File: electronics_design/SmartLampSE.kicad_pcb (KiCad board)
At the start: 2 copper layers, 15 parts, among them J1 Screw_Terminal_01x02, M1 PIC16F886-IP, U1 L7805, Y1 Crystal

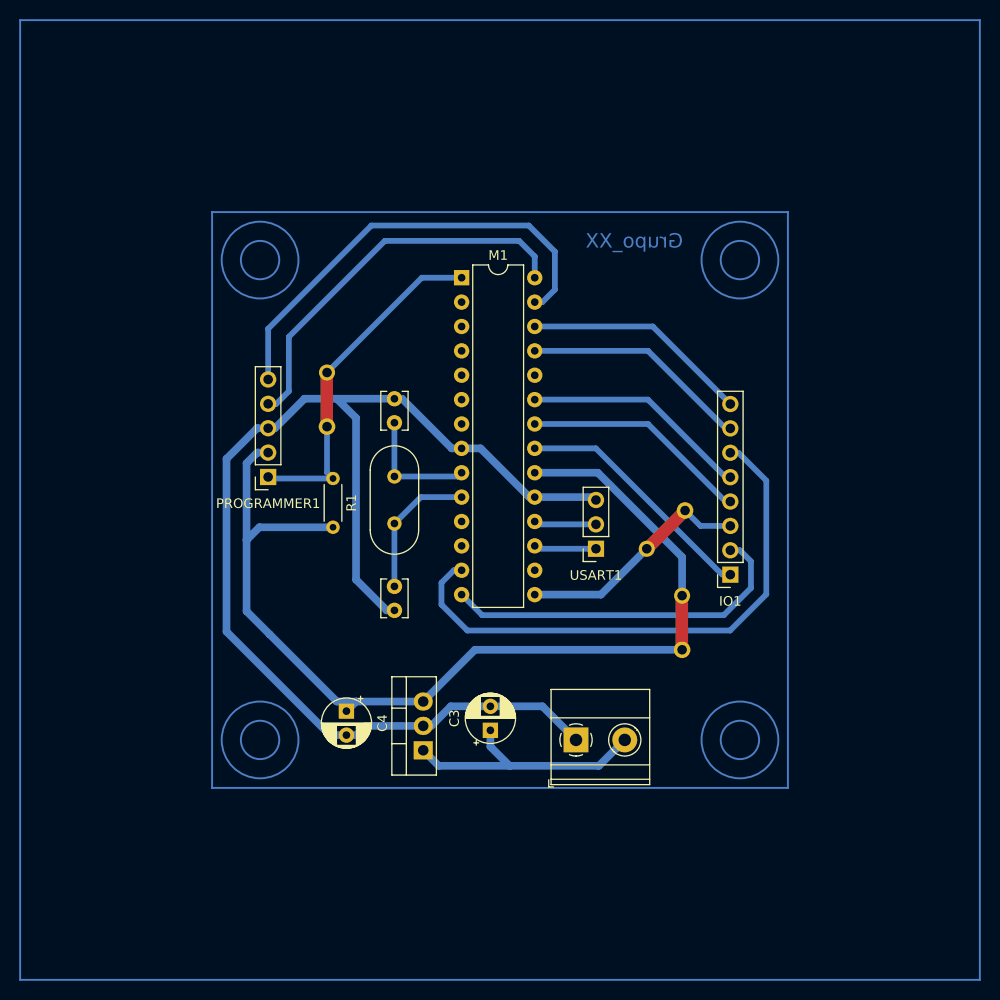
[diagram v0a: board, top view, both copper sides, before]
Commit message: Separate board IO interface
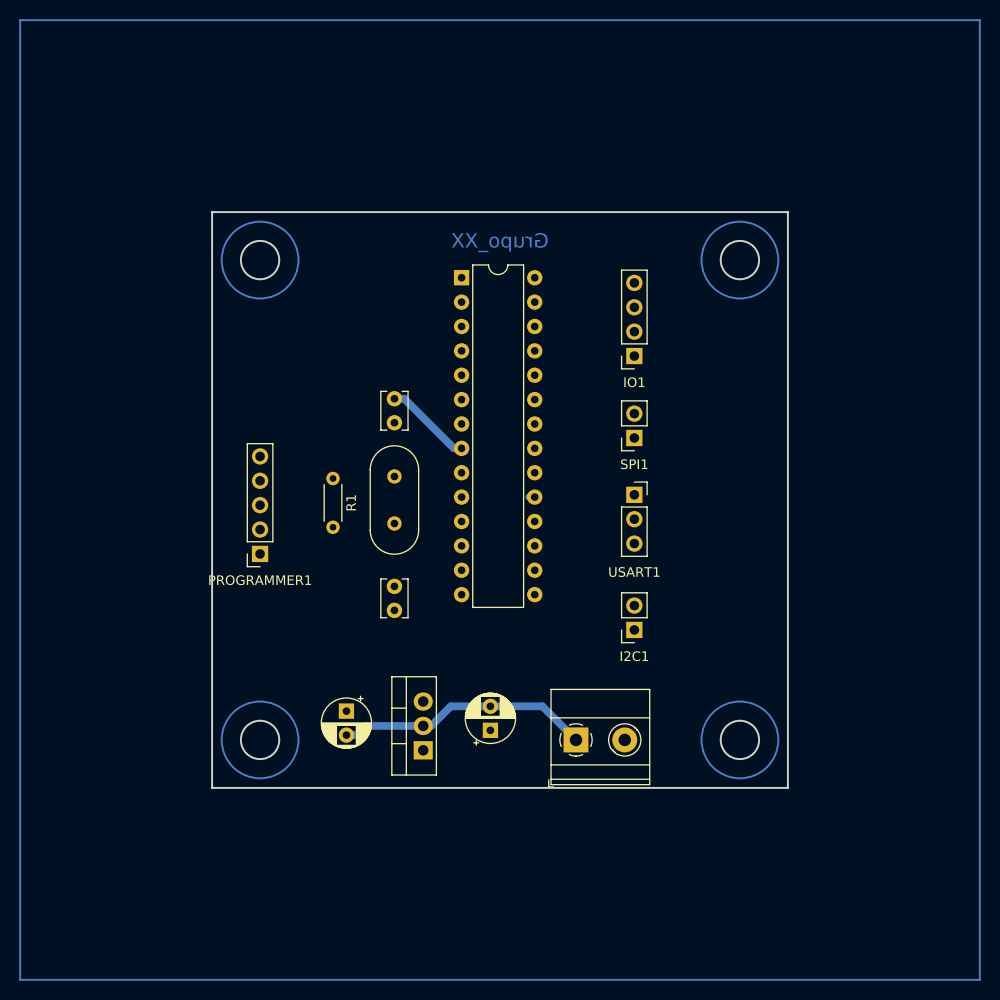
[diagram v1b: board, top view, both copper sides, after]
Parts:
- removed NT1, NT3: NetTie_2, Custom_Library:NetTie-2_THT_Custom_Pad1.0mm
- removed NT2: NetTie_2, NetTie:NetTie-2_THT_Pad1.0mm
- added I2C1: Conn_01x02, Connector_PinSocket_2.54mm:PinSocket_1x02_P2.54mm_Vertical, F.Cu at (155.0, 117.5)
- added SPI1: Conn_01x02, Connector_PinSocket_2.54mm:PinSocket_1x02_P2.54mm_Vertical, F.Cu at (155.0, 97.5)
- IO1: value Conn_01x08 -> Conn_01x04; footprint Connector_PinSocket_2.54mm:PinSocket_1x08_P2.54mm_Vertical -> Connector_PinSocket_2.54mm:PinSocket_1x04_P2.54mm_Vertical
- moved IO1 24.9 mm to (155.0, 89.0)
- moved PROGRAMMER1 8.06 mm to (116.0, 109.6)
- moved USART1 6.90 mm to (155.0, 103.5), turned to 0 degrees
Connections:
- M1 pad 1: Net-(M1-RE3/~{MCLR}/Vpp) -> mclr
- M1 pad 13: Net-(IO1-Pin_6) -> Net-(IO1-Pin_4)
- M1 pad 14: Net-(IO1-Pin_2) -> Net-(I2C1-Pin_1)
- M1 pad 20: Net-(M1-VDD) -> +5V
- M1 pad 22: Net-(IO1-Pin_4) -> Net-(IO1-Pin_2)
- M1 pad 23: Net-(IO1-Pin_5) -> Net-(IO1-Pin_3)
- M1 pad 25: Net-(IO1-Pin_7) -> Net-(M1-P1D/AN11/RB4)
- M1 pad 26: Net-(IO1-Pin_8) -> Net-(M1-~{T1G}/AN13/RB5)
- USART1 pad 1: Net-(M1-RC6/TX/CK) -> GND
- USART1 pad 3: GND -> Net-(M1-RC6/TX/CK)
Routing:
- net GND: track 132.1 -> 36.3 mm
- net +5V: track 80.6 -> 0.00 mm
- net Net-(IO1-Pin_6): track 58.3 -> 0.00 mm
- net icsp_clk: track 47.3 -> 0.00 mm
- net icsp_dat: track 41.0 -> 0.00 mm
- net Net-(IO1-Pin_2): track 37.6 -> 0.00 mm
- net +12V: track 27.3 -> 0.00 mm
- net Net-(IO1-Pin_1): track 25.8 -> 0.00 mm
- net Net-(IO1-Pin_7): track 23.7 -> 0.00 mm
- net Net-(IO1-Pin_8): track 23.7 -> 0.00 mm
- net Net-(IO1-Pin_5): track 23.7 -> 0.00 mm
- net Net-(IO1-Pin_4): track 23.7 -> 0.00 mm
- net Net-(M1-VDD): track 23.0 -> 0.00 mm
- net Net-(M1-RE3/~{MCLR}/Vpp): track 18.1 -> 0.00 mm
- net Net-(M1-CLKOUT/OSC2/RA6): track 14.7 -> 0.00 mm
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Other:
- board outline added: 60 x 60 mm

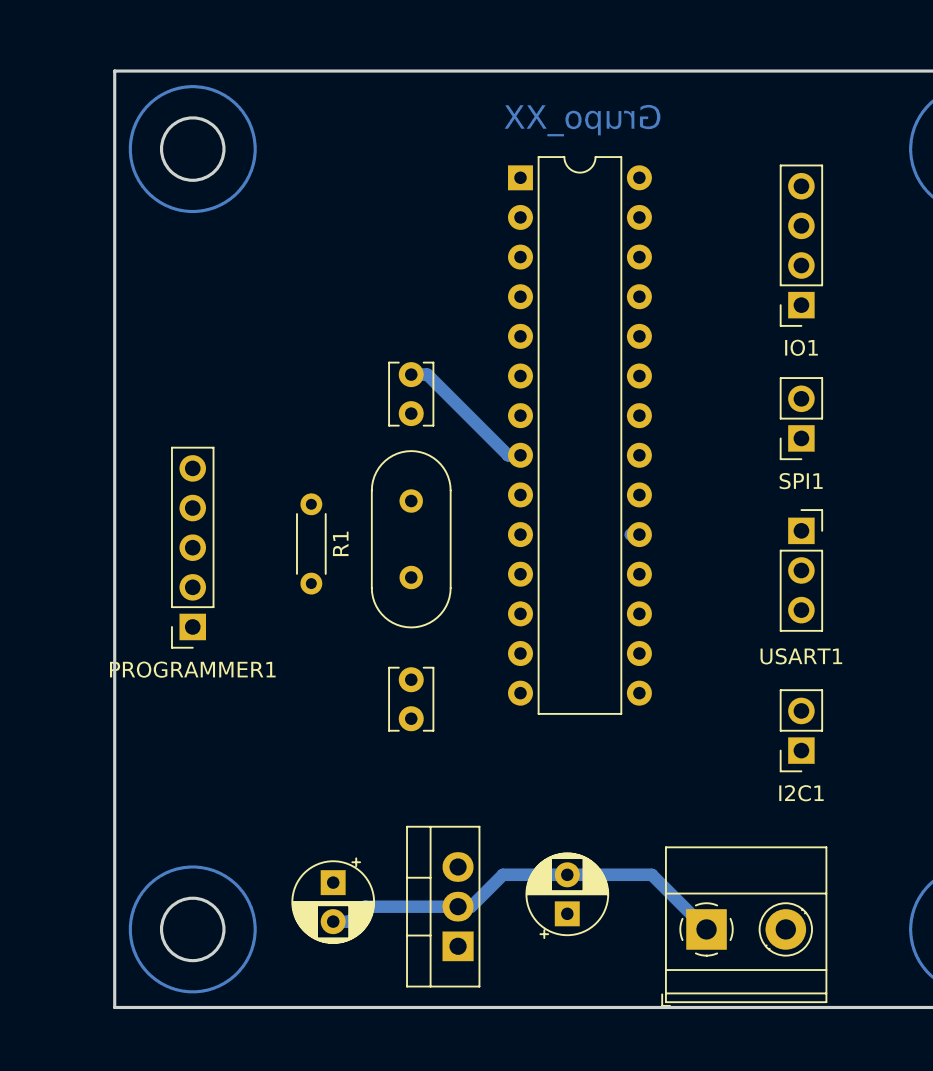
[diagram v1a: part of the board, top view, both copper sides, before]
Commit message: Separate board IO interface
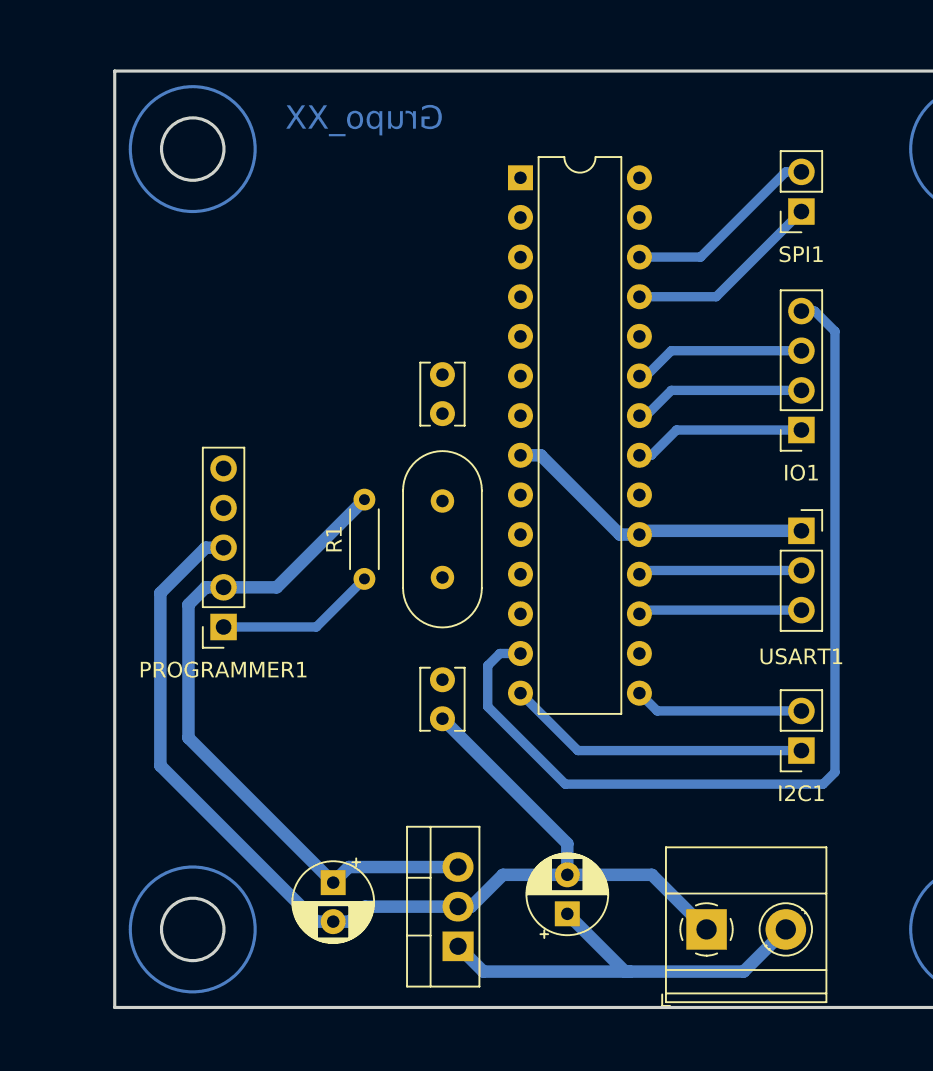
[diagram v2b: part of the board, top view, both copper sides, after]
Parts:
- moved SPI1 14.5 mm to (155.0, 83.0)
- moved IO1 8.00 mm to (155.0, 97.0)
- moved R1 5.87 mm to (127.0, 106.5), turned to 90 degrees
- moved C1 2.00 mm to (132.0, 113.0)
- moved C2 2.00 mm to (132.0, 96.0)
- moved Y1 2.00 mm to (132.0, 101.5)
- moved PROGRAMMER1 1.97 mm to (118.0, 109.6)
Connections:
- net Net-(I2C1-Pin_1) renamed signal_i2c_scl
- net Net-(I2C1-Pin_2) renamed signal_i2c_sda
- net Net-(IO1-Pin_1) renamed signal_an12
- net Net-(IO1-Pin_2) renamed signal_an10
- net Net-(IO1-Pin_3) renamed signal_an8
- net Net-(IO1-Pin_4) renamed signal_pwm
- net Net-(M1-CLKIN/OSC1/RA7) renamed signal_clkin
- net Net-(M1-CLKOUT/OSC2/RA6) renamed signal_clkout
- net Net-(M1-P1D/AN11/RB4) renamed signal_spi_sck
- net Net-(M1-RC6/TX/CK) renamed signal_tx
- net Net-(M1-RC7/RX/DT) renamed signal_rx
- net Net-(M1-~{T1G}/AN13/RB5) renamed signal_spi_sdo
- net icsp_clk renamed signal_icsp_clk
- net icsp_dat renamed signal_icsp_dat
- net mclr renamed signal_mclr
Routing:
- net signal_pwm: track 0.00 -> 60.6 mm
- net GND: track 36.3 -> 91.7 mm
- net +5V: track 0.00 -> 44.1 mm
- net +12V: track 0.00 -> 28.3 mm
- net signal_i2c_scl: track 0.00 -> 19.5 mm
- net signal_spi_sdo: track 0.00 -> 12.6 mm
- net signal_spi_sck: track 0.00 -> 12.6 mm
- net signal_an8: track 0.00 -> 11.1 mm
- net signal_an12: track 0.00 -> 11.1 mm
- net signal_an10: track 0.00 -> 11.1 mm
- net signal_i2c_sda: track 0.00 -> 10.9 mm
- net signal_tx: track 0.00 -> 10.5 mm
- net signal_rx: track 0.00 -> 10.5 mm
- net signal_mclr: track 0.00 -> 10.3 mm

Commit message: Finish pcb pathing
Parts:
- moved J1 36.9 mm to (116.9, 110.6), turned to -90 degrees
- moved U1 35.1 mm to (116.5, 99.1)
- moved PROGRAMMER1 34.7 mm to (135.9, 80.0), turned to 90 degrees
- moved C4 33.2 mm to (123.0, 92.8)
- moved C3 30.1 mm to (123.0, 103.2)
- moved R1 18.1 mm to (130.9, 88.9), turned to -90 degrees
- moved I2C1 8.95 mm to (156.0, 126.4)
- moved IO1 8.68 mm to (156.0, 105.6)
- moved USART1 8.52 mm to (156.0, 111.9)
- moved SPI1 8.06 mm to (156.0, 91.0)
- moved M1 7.62 mm to (137.0, 88.5)
- moved Y1 6.98 mm to (130.3, 108.3)
- moved C1 6.54 mm to (130.3, 119.3)
- moved C2 5.63 mm to (130.3, 101.3)
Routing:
- net GND: track 91.7 -> 137.6 mm
- net +5V: track 44.1 -> 73.0 mm
- net signal_pwm: track 60.6 -> 80.6 mm
- net signal_clkin: track 0.00 -> 13.9 mm
- net signal_clkout: track 0.00 -> 13.6 mm
- net signal_icsp_clk: track 0.00 -> 12.6 mm
- net signal_icsp_dat: track 0.00 -> 8.92 mm
- net +12V: track 28.3 -> 33.7 mm
- net signal_mclr: track 10.3 -> 15.1 mm
- net signal_rx: track 10.5 -> 12.9 mm
- net signal_i2c_sda: track 10.9 -> 13.2 mm
- net signal_tx: track 10.5 -> 12.1 mm
- net signal_i2c_scl: track 19.5 -> 21.1 mm
- net signal_an10: track 11.1 -> 12.0 mm
- net signal_an12: track 11.1 -> 12.0 mm
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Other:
- board text added: "AN08"
- board text added: "AN10"
- board text added: "AN12"
- board text added: "CCMP1"
- board text added: "GND(B)"
- board text added: "I2C"
- board text added: "IO"
- board text added: "PIN1"
- board text added: "RB4"
- board text added: "RB5"
- board text added: "RX(O)"
- board text added: "SCK"
- board text added: "SCL"
- board text added: "SDA"
- board text added: "SDO"
- board text added: "SPI"
- board text added: "TRIANGLE POINTS TO PIN1"
- board text added: "TX(Y)"
- board text added: "UART"
- board text added: "↓"

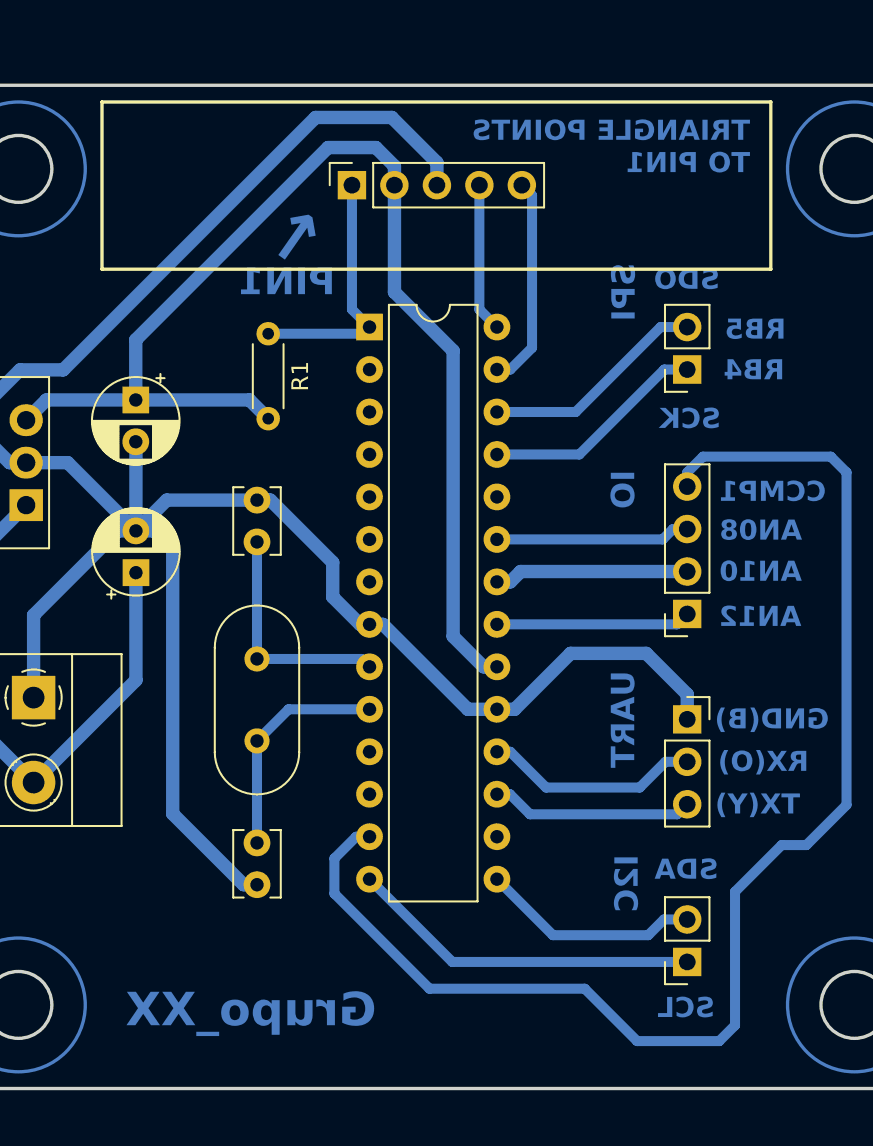
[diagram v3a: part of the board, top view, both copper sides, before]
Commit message: Update group name on electronics design
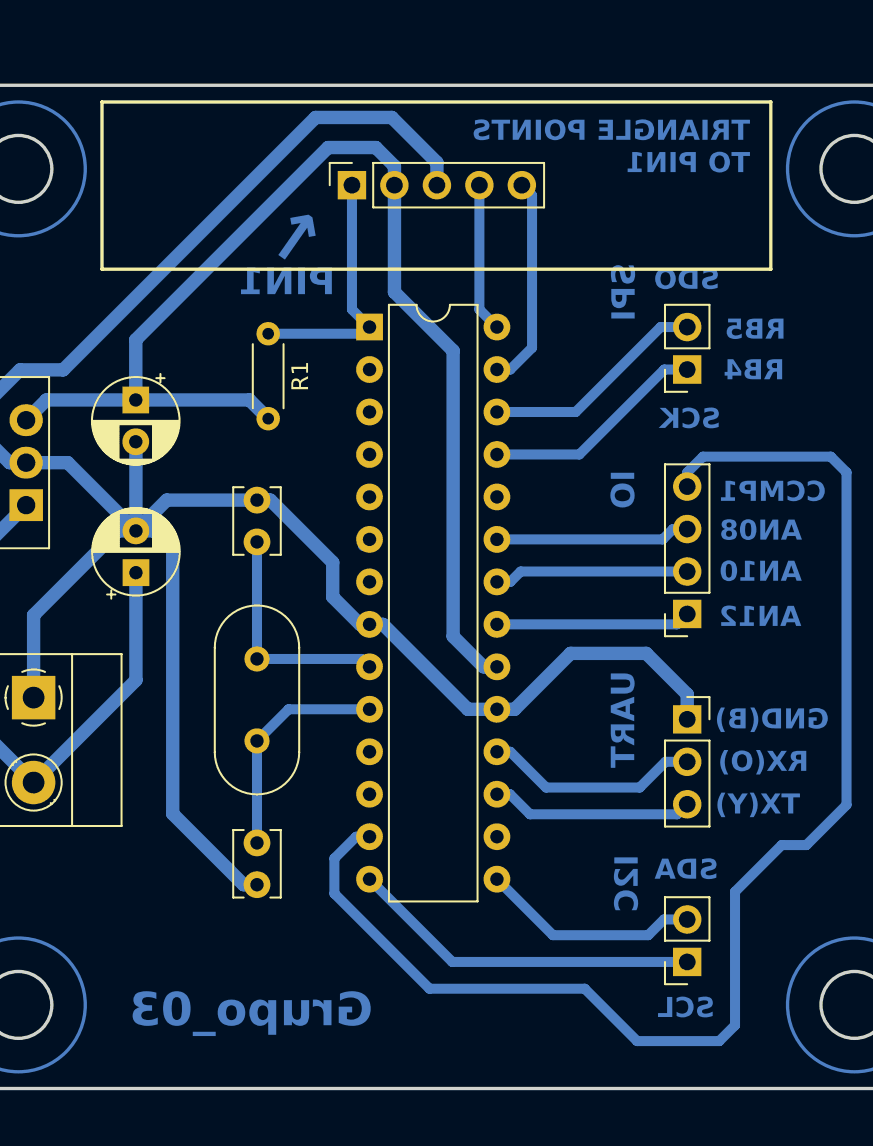
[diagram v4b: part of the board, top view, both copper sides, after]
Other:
- board text added: "Grupo_03"
- board text removed: "Grupo_XX"
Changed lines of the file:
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@@
   (gr_circle (center 166 129) (end 166 133)
     (stroke (width 0.2) (type solid)) (fill none) (layer "B.Cu"))
-  (gr_rect (start 121 85) (end 161 75)
+  (gr_rect (start 121 75) (end 161 85)
     (stroke (width 0.2) (type default)) (fill none) (layer "F.SilkS"))
   (gr_circle (center 166 79) (end 168 79)
@@
     (effects (font (size 1.4 1.4) (thickness 0.3) bold) (justify left bottom mirror))
   )
-  (gr_text "Grupo_XX" (at 129.91 129.29) (layer "B.Cu")
+  (gr_text "Grupo_03" (at 129.91 129.29) (layer "B.Cu")
     (effects (font (size 2 2) (thickness 0.5) bold) (justify mirror))
   )
@@
   (segment (start 116.465 94.03) (end 117.675 92.82) (width 0.8) (layer "B.Cu") (net 5))
   (segment (start 137.3799 77.725) (end 138.49 78.8351) (width 0.8) (layer "B.Cu") (net 5))
-  (segment (start 144.86 108.54) (end 144.62 108.78) (width 0.6) (layer "B.Cu") (net 5))
+  (segment (start 144.86 108.54) (end 144.62 108.78) (width 0.8) (layer "B.Cu") (net 5))
   (segment (start 123.02 92.82) (end 129.82 92.82) (width 0.8) (layer "B.Cu") (net 5))
   (segment (start 134.5201 77.725) (end 137.3799 77.725) (width 0.8) (layer "B.Cu") (net 5))
@@
   (segment (start 144.86 106) (end 144.62 106.24) (width 0.6) (layer "B.Cu") (net 8))
   (segment (start 155.38 106.24) (end 144.62 106.24) (width 0.6) (layer "B.Cu") (net 8))
-  (segment (start 144.86 103.46) (end 144.62 103.7) (width 0.8) (layer "B.Cu") (net 9))
-  (segment (start 144.62 103.7) (end 145.42 103.7) (width 0.8) (layer "B.Cu") (net 9))
-  (segment (start 145.42 103.7) (end 146.04 103.08) (width 0.8) (layer "B.Cu") (net 9))
-  (segment (start 146.04 103.08) (end 156 103.08) (width 0.8) (layer "B.Cu") (net 9))
+  (segment (start 144.86 103.46) (end 144.62 103.7) (width 0.6) (layer "B.Cu") (net 9))
+  (segment (start 144.62 103.7) (end 145.42 103.7) (width 0.6) (layer "B.Cu") (net 9))
+  (segment (start 145.42 103.7) (end 146.04 103.08) (width 0.6) (layer "B.Cu") (net 9))
+  (segment (start 146.04 103.08) (end 156 103.08) (width 0.6) (layer "B.Cu") (net 9))
   (segment (start 154.53 101.16) (end 144.62 101.16) (width 0.6) (layer "B.Cu") (net 10))
   (segment (start 156 100.54) (end 155.15 100.54) (width 0.6) (layer "B.Cu") (net 10))
